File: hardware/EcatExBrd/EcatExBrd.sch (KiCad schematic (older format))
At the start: 17 parts, among them J1 Conn_01x03, U1 OPA388

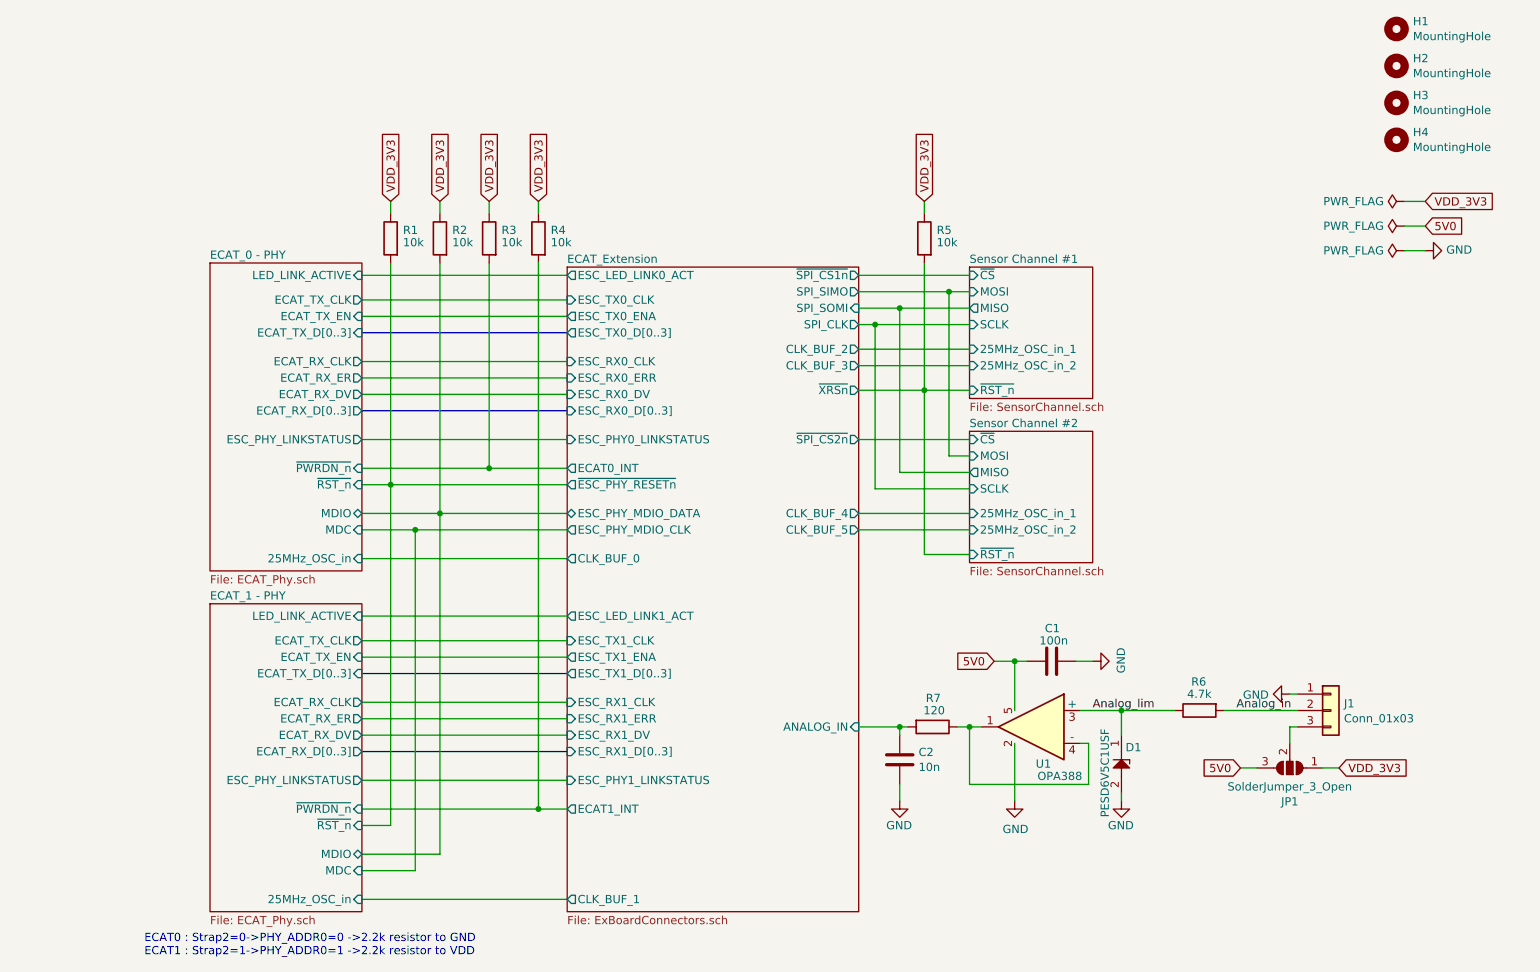
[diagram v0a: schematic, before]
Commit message: µOmodri extension board PCB routing update with gerber files.
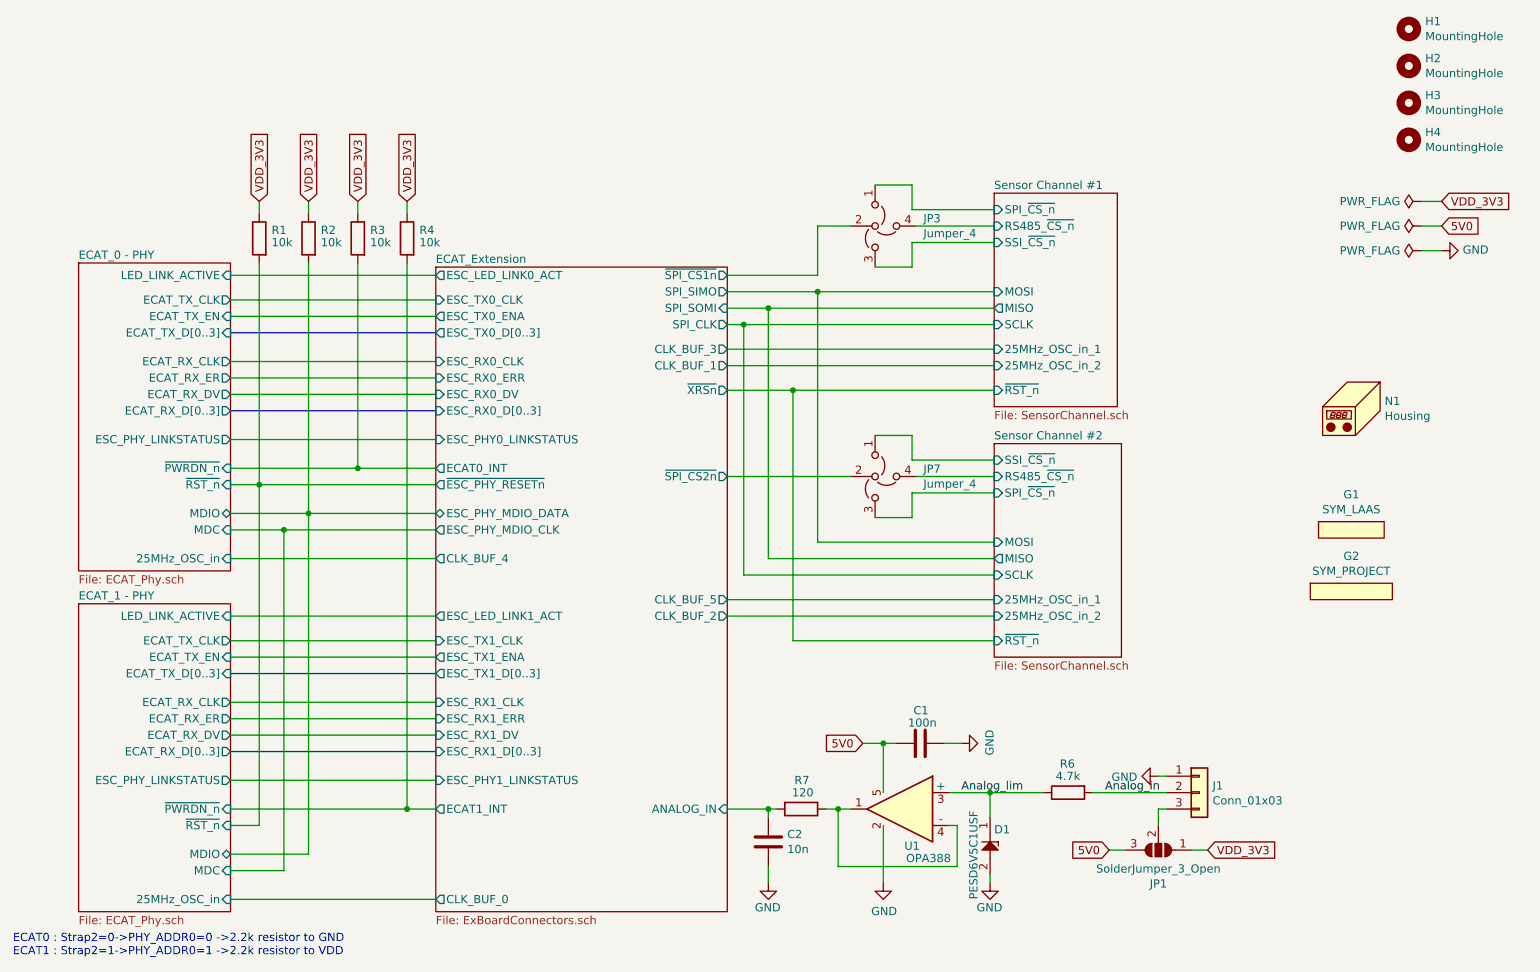
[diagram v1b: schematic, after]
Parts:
- removed R5: 10k, Resistor_SMD:R_0201_0603Metric, symbol Device:R
- added G1: SYM_LAAS, EcatExBrd:logo_laas, symbol ecatextbrd_lib:SYM_LAAS
- added G2: SYM_PROJECT, EcatExBrd:logo_OpenHardware, symbol ecatextbrd_lib:SYM_PROJECT
- added JP3, JP7: Jumper_4, EcatExBrd:Harwin_M50_04_P1.27mm_cross_Vertical, symbol ecatextbrd_lib:Jumper_4
- added N1: Housing, EcatExBrd:uOmodri_laas, symbol Mechanical:Housing
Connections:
- net ECAT_Extension/~SPI_CS1n~: now also JP3.2 (C)
- net ECAT_Extension/~SPI_CS2n~: now also JP7.2 (C)
- new net Sensor Channel #1/RS485_~CS_n~: JP3.4 (A)
- new net Sensor Channel #1/SPI_~CS_n~: JP3.1 (A)
- new net Sensor Channel #1/SSI_~CS_n~: JP3.3 (B)
- new net Sensor Channel #2/RS485_~CS_n~: JP7.4 (A)
- new net Sensor Channel #2/SPI_~CS_n~: JP7.3 (B)
- new net Sensor Channel #2/SSI_~CS_n~: JP7.1 (A)
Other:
- moved on the sheet: C1, C2, D1, H1, H2, H3, H4, J1, JP1, R1, R2, R3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
